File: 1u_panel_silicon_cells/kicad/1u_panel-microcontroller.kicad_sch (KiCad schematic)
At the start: 43 parts, among them J2 2-1734592-0, U1 TCAN330GDCNT, U11 TMP101NA/3KSLOTTED, U2 TMP101NA/3KSLOTTED, U7 STM32F091CCT7, X1 ECS-160-10-36Q-ES-TR

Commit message: final changes for silicon solar module
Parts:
- X1: footprint Crystal:Crystal_SMD_2520-4Pin_2.5x2.0mm -> oresat-misc:ECS-160-10-36Q-ES-TR; symbol Device:Crystal_GND2 -> Device:Crystal_GND24
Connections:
- net GND: now also X1.4
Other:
- moved on the sheet: C28
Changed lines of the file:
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@@
 	(wire
 		(pts
-			(xy 166.37 115.57) (xy 166.37 96.52)
+			(xy 158.75 115.57) (xy 158.75 96.52)
 		)
 		(stroke
@@
 	(wire
 		(pts
-			(xy 166.37 127) (xy 166.37 129.54)
+			(xy 158.75 127) (xy 158.75 129.54)
 		)
 		(stroke
@@
 	(wire
 		(pts
+			(xy 166.37 101.6) (xy 166.37 129.54)
+		)
+		(stroke
+			(width 0)
+			(type default)
+		)
+	)
+	(wire
+		(pts
 			(xy 250.19 73.66) (xy 250.19 76.2)
 		)
@@
 	(wire
 		(pts
+			(xy 168.91 101.6) (xy 166.37 101.6)
+		)
+		(stroke
+			(width 0)
+			(type default)
+		)
+	)
+	(wire
+		(pts
 			(xy 299.72 184.15) (xy 110.49 184.15)
 		)
@@
 	(wire
 		(pts
-			(xy 166.37 96.52) (xy 173.99 96.52)
+			(xy 158.75 96.52) (xy 173.99 96.52)
 		)
 		(stroke
@@
 	(wire
 		(pts
-			(xy 166.37 127) (xy 166.37 123.19)
+			(xy 158.75 127) (xy 158.75 123.19)
 		)
 		(stroke
@@
 	(text "NP0 Dielectric"
 		(exclude_from_sim no)
-		(at 163.576 112.776 90)
+		(at 156.21 112.268 90)
 		(effects
 			(font
@@
 	(symbol
 		(lib_id "oresat-power:GND")
+		(at 166.37 129.54 0)
+		(mirror y)
+		(unit 1)
+		(exclude_from_sim no)
+		(in_bom yes)
+		(on_board yes)
+		(dnp no)
+		(property "Reference" "#GND010"
+			(at 166.37 129.54 0)
+			(effects
+				(font
+					(size 1.27 1.27)
+				)
+				(hide yes)
+			)
+		)
+		(property "Value" "GND"
+			(at 168.402 133.35 0)
+			(effects
+				(font
+					(size 1.778 1.27)
+				)
+				(justify left bottom)
+			)
+		)
+		(property "Footprint" ""
+			(at 166.37 130.81 0)
+			(effects
+				(font
+					(size 1.27 1.27)
+				)
+				(hide yes)
+			)
+		)
+		(property "Datasheet" ""
+			(at 166.37 130.81 0)
+			(effects
+				(font
+					(size 1.27 1.27)
+				)
+				(hide yes)
+			)
+		)
+		(property "Description" "Power symbol creates a global label with name \"GND\" , ground"
+			(at 166.37 129.54 0)
+			(effects
+				(font
+					(size 1.27 1.27)
+				)
+				(hide yes)
+			)
+		)
+		(pin "1"
+		)
+		(instances
+			(project "1u_panel-silicon"
+				(path "/115bd2cd-7c08-4b54-867b-a326ee0699c1/bfa81e66-0bc2-4d21-a09c-e64719ae80bc"
+					(reference "#GND010")
+					(unit 1)
+				)
+			)
+		)
+	)
+	(symbol
+		(lib_id "oresat-power:GND")
 		(at 215.9 233.68 0)
 		(mirror y)
@@
 	)
 	(symbol
-		(lib_id "Device:Crystal_GND2")
+		(lib_id "Device:Crystal_GND24")
 		(at 173.99 101.6 90)
 		(mirror x)
@@
 			)
 		)
-		(property "Footprint" "Crystal:Crystal_SMD_2520-4Pin_2.5x2.0mm"
+		(property "Footprint" "oresat-misc:ECS-160-10-36Q-ES-TR"
 			(at 173.99 101.6 0)
 			(effects
@@
 			)
 		)
-		(property "Description" "Three pin crystal, GND on pin 2"
+		(property "Description" "Four pin crystal, GND on pins 2 and 4"
 			(at 173.99 101.6 0)
 			(effects
@@
 		(pin "3"
 		)
+		(pin "4"
+		)
 		(instances
 			(project "1u_panel-silicon"
@@
 	(symbol
 		(lib_id "Device:C")
-		(at 166.37 119.38 0)
+		(at 158.75 119.38 0)
 		(mirror y)
 		(unit 1)
@@
 		(dnp no)
 		(property "Reference" "C28"
-			(at 164.846 117.856 0)
+			(at 157.226 117.856 0)
 			(effects
 				(font
@@
 		)
 		(property "Value" "20p"
-			(at 164.846 122.936 0)
+			(at 157.226 122.936 0)
 			(effects
 				(font
@@
 		)
 		(property "Footprint" "oresat-passives:0603-C-NOSILK"
-			(at 165.4048 123.19 0)
+			(at 157.7848 123.19 0)
 			(effects
 				(font
@@
 		)
 		(property "Datasheet" "~"
-			(at 166.37 119.38 0)
+			(at 158.75 119.38 0)
 			(effects
 				(font
@@
 		)
 		(property "Description" "Unpolarized capacitor"
-			(at 166.37 119.38 0)
+			(at 158.75 119.38 0)
 			(effects
 				(font
@@
 		)
 		(property "DIS" "Digi-Key"
-			(at 166.37 119.38 0)
+			(at 158.75 119.38 0)
 			(effects
 				(font
@@
 		)
 		(property "DPN" "490-1334-2-ND"
-			(at 166.37 119.38 0)
+			(at 158.75 119.38 0)
 			(effects
 				(font
@@
 		)
 		(property "MFR" "Murata"
-			(at 166.37 119.38 0)
+			(at 158.75 119.38 0)
 			(effects
 				(font
@@
 		)
 		(property "MPN" "GRM1885C2A200JA01D"
-			(at 166.37 119.38 0)
+			(at 158.75 119.38 0)
 			(effects
 				(font
@@
 		)
 		(instances
-			(project "1u_panel-silicon"
+			(project ""
+				(path "/115bd2cd-7c08-4b54-867b-a326ee0699c1/5c4415f1-d90e-44ce-bb2c-b4c8edead48f"
+					(reference "C9")
+					(unit 1)
+				)
 				(path "/115bd2cd-7c08-4b54-867b-a326ee0699c1/bfa81e66-0bc2-4d21-a09c-e64719ae80bc"
 					(reference "C9")
@@
 	(symbol
 		(lib_id "oresat-power:GND")
-		(at 166.37 129.54 0)
+		(at 158.75 129.54 0)
 		(mirror y)
 		(unit 1)
@@
 		(dnp no)
 		(property "Reference" "#GND054"
-			(at 166.37 129.54 0)
+			(at 158.75 129.54 0)
 			(effects
 				(font
@@
 		)
 		(property "Value" "GND"
-			(at 168.402 133.35 0)
+			(at 160.782 133.35 0)
 			(effects
 				(font
@@
 		)
 		(property "Footprint" ""
-			(at 166.37 130.81 0)
+			(at 158.75 130.81 0)
 			(effects
 				(font
@@
 		)
 		(property "Datasheet" ""
-			(at 166.37 130.81 0)
+			(at 158.75 130.81 0)
 			(effects
 				(font
@@
 		)
 		(property "Description" "Power symbol creates a global label with name \"GND\" , ground"
-			(at 166.37 129.54 0)
+			(at 158.75 129.54 0)
 			(effects
 				(font

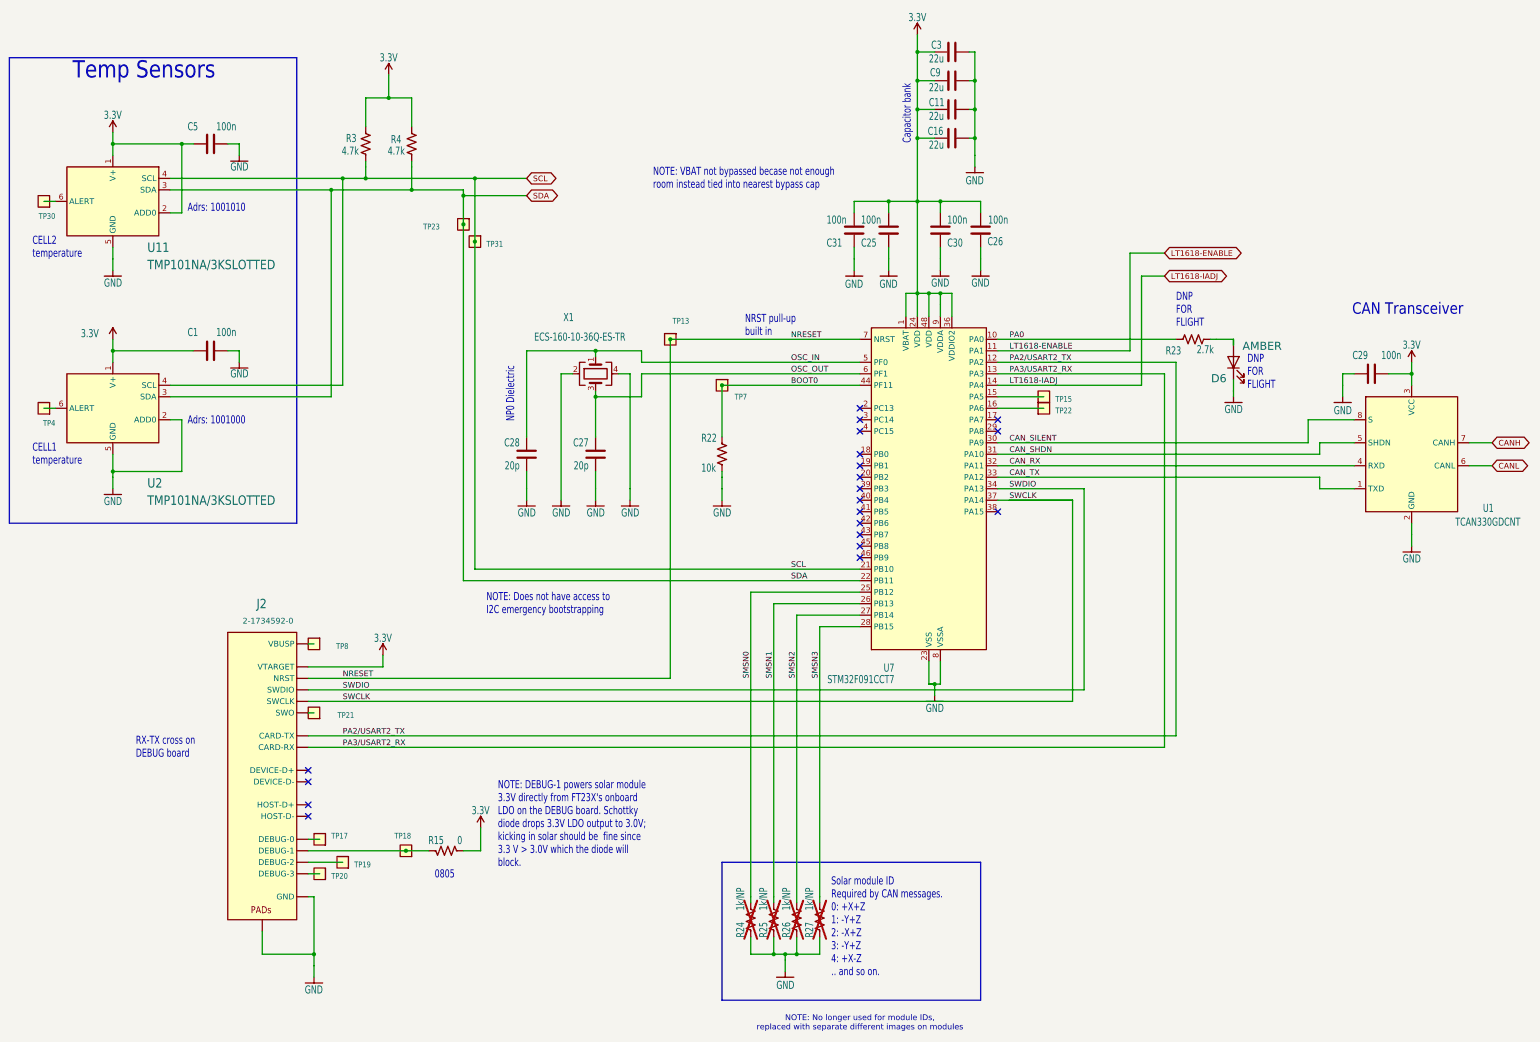
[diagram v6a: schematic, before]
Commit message: Polish on Jack's final design. Swapped out rectangles for zones on multiple layers, cleaned up a lot of small layout bits, fixed some mechanical crashes with screw heads, fixed up the silk screen, and added 3D models.
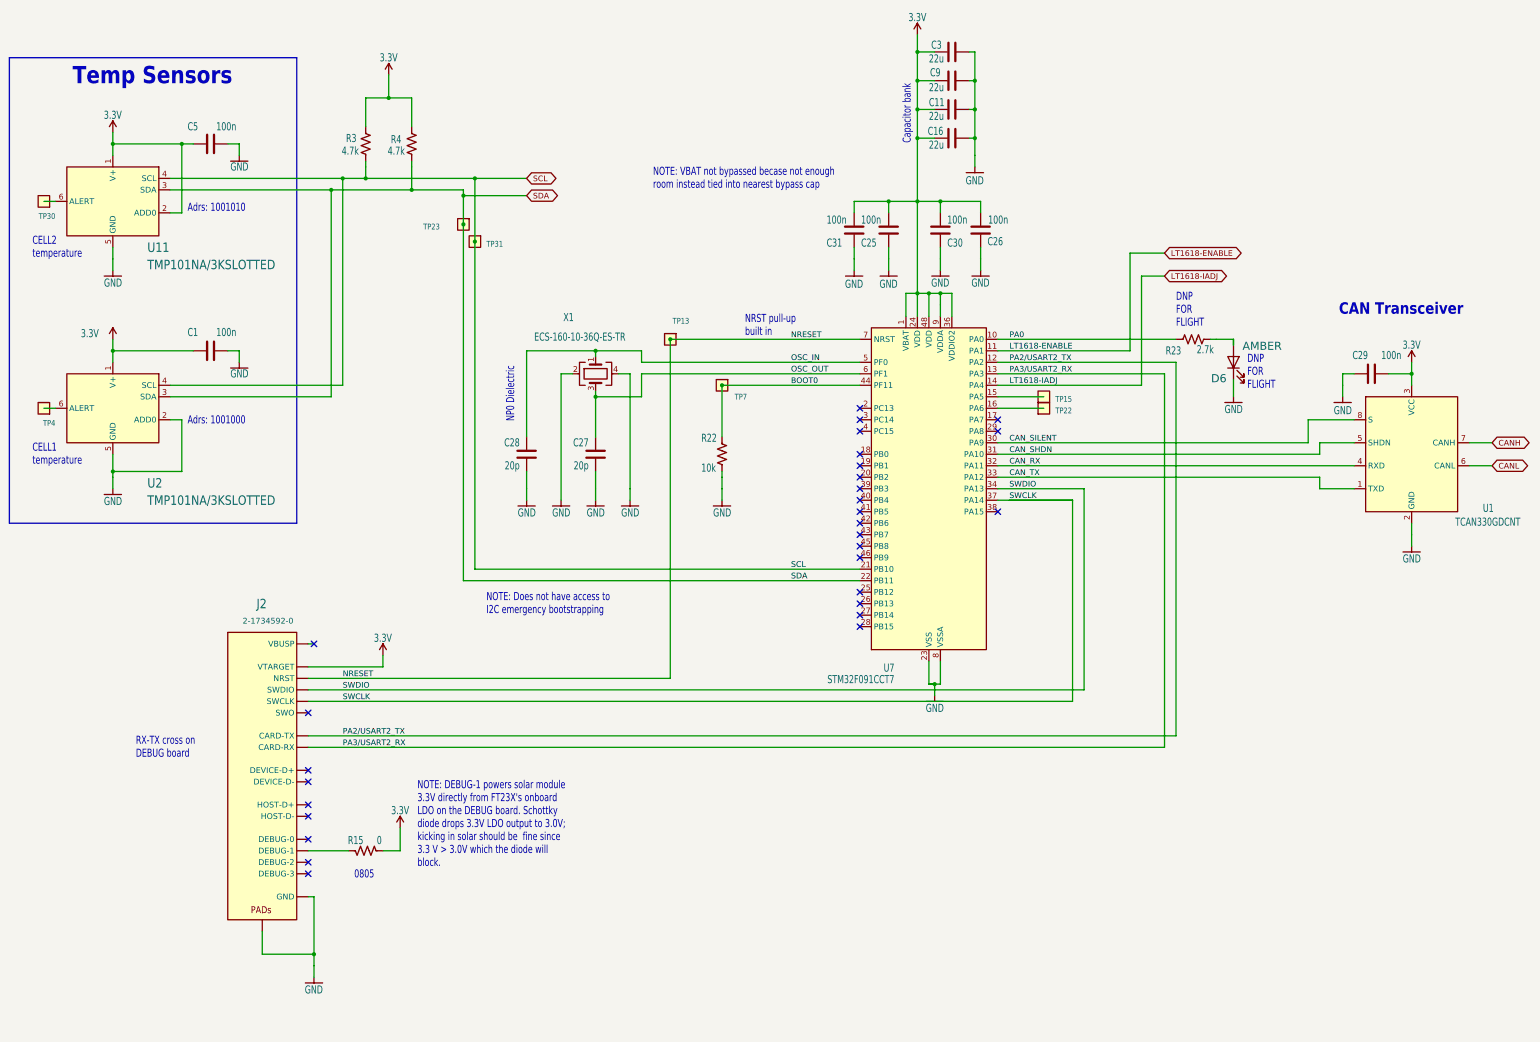
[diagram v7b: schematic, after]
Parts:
- removed R24, R25, R26, R27: 1k/NP, oresat-passives:0603-C-NOSILK, symbol Device:R_US
- removed TP17, TP18, TP19, TP20, TP21, TP8: TEST-POINT-LARGE-SQUARE, oresat-misc:TestPoint-0.75mm-th, symbol oresat-misc:Test-Point-0.75mm-th
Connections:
- net SMSN0: no longer names the net of U7.25 (PB12)
- net SMSN1: no longer names the net of U7.26 (PB13)
- net SMSN2: no longer names the net of U7.27 (PB14)
- net SMSN3: no longer names the net of U7.28 (PB15)
- no-connect marks 20 -> 29
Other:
- note removed: "NOTE: No longer used for module IDs, replaced with separate different images on modules"
- note removed: "Solar module ID Required by CAN messages. 0: +X+Z 1: -Y+Z 2: -X+Z 3: -Y+Z 4: +X-Z .. and so on."
- title: OreSat Silicon Solar Module (for Frame 2.0) -> OreSat Solar Module - Silicon Cells
- moved on the sheet: R15

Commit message: updated part numbers for all components on silicon module to be flight-ready hardware PNs, pulled from CFC mfr series'
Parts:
- C1, C25, C26, C29, C30, C31, C5: DPN 490-5798-2-ND -> 399-C0603C101J5GAC3190CT-ND; Distributor (none) -> Digi-Key; MFR Murata -> KEMET; MPN GCJ188R71H104KA12D -> C0603C101J5GAC3190
- C11, C16, C3, C9: DPN 2571-GMC21X7R226M10NTTR-ND -> 490-GRT21BC81C226ME13KTR-ND; Distributor (none) -> Digi-Key; MFR Cal-Chip -> Murata; MPN GMC21X7R226M10NT -> GRT21BC81C226ME13K
- C27, C28: DPN 490-1334-2-ND -> 399-15921-2-ND; Distributor (none) -> Digi-Key; MFR Murata -> KEMET; MPN GRM1885C2A200JA01D -> C0603C200J5GACAUTO
- D6: DPN 1830-1064-1-ND -> 732-150060AS75000TR-ND; Distributor (none) -> Digi-Key; MFR Inolux -> Wurth; MPN IN-S63AT5A -> 150060AS75000
- J2: DPN A100287TR-ND -> A100287CT-ND; Distributor (none) -> Digi-Key; MFR TE -> TE Connectivity AMP Connectors
- R15: DPN RMCF0805ZT0R00CT-ND -> P0.0ATR-ND; Distributor (none) -> Digi-Key; MFR Stackpole -> Panasonic; MPN RMCF0805ZT0R00 -> ERJ-6GEY0R00V
- R22: DPN RMCF0603JT10K0 -> RMCF0603FT10K0CT-ND; Distributor (none) -> Digi-Key; MFR Stackpole -> Stackpole Electronics Inc; MPN RMCF0603JT10K0 -> RMCF0603FT10K0
- R23: DPN A129693CT-ND -> RMCF0603FT2K70TR-ND; Distributor (none) -> Digi-Key; MFR TE -> Stackpole Electronics Inc; MPN CRGCQ0603F2K7 -> RMCF0603FT2K70
- R3, R4: DPN 13-RE0603FRE074K7LCT-ND -> RMCF0603FT4K70CT-ND; Distributor (none) -> Digi-Key; MFR Yageo -> Stackpole Electronics Inc; MPN RE0603FRE074K7L -> RMCF0603FT4K70
- U1: Distributor DigiKey -> Digi-Key; MPN TCAN330GDCN -> TCAN330GDCNT
- U11, U2: DPN 296-27725-1-ND -> 296-27725-2-ND; Distributor (none) -> Digi-Key
- U7: DPN 497-18749-1-ND -> STM32F091CCT7TR; Distributor (none) -> Digi-Key; MPN STM32F091CCT6TR -> STM32F091CCT7TR
- X1: DPN XC2181CT-ND -> XC2181TR-ND; Distributor (none) -> Digi-Key
